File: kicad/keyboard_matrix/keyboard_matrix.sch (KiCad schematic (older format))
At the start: 21 parts, among them J1 Conn_01x09, SW1 SPST, SW10 SPST, SW11 SPST, SW12 SPST, SW13 SPST, SW14 SPST, SW15 SPST, SW16 SPST, SW17 SPST, SW18 SPST, SW19 SPST, SW2 SPST, SW20 SPST, SW3 SPST, SW4 SPST, SW5 SPST, SW6 SPST, SW7 SPST, SW8 SPST, SW9 SPST

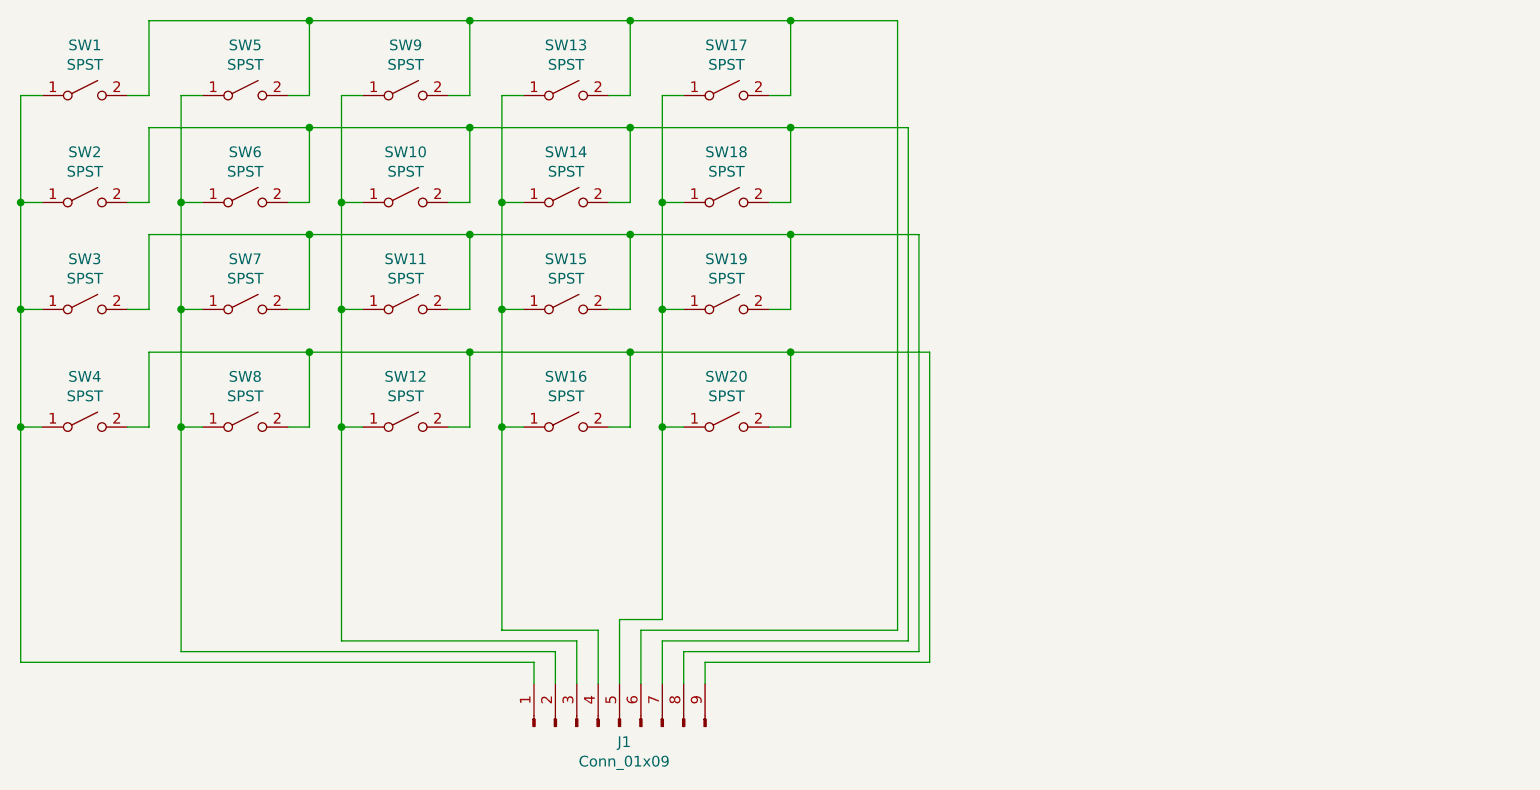
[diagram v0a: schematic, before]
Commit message: Try labels on matrix schematic
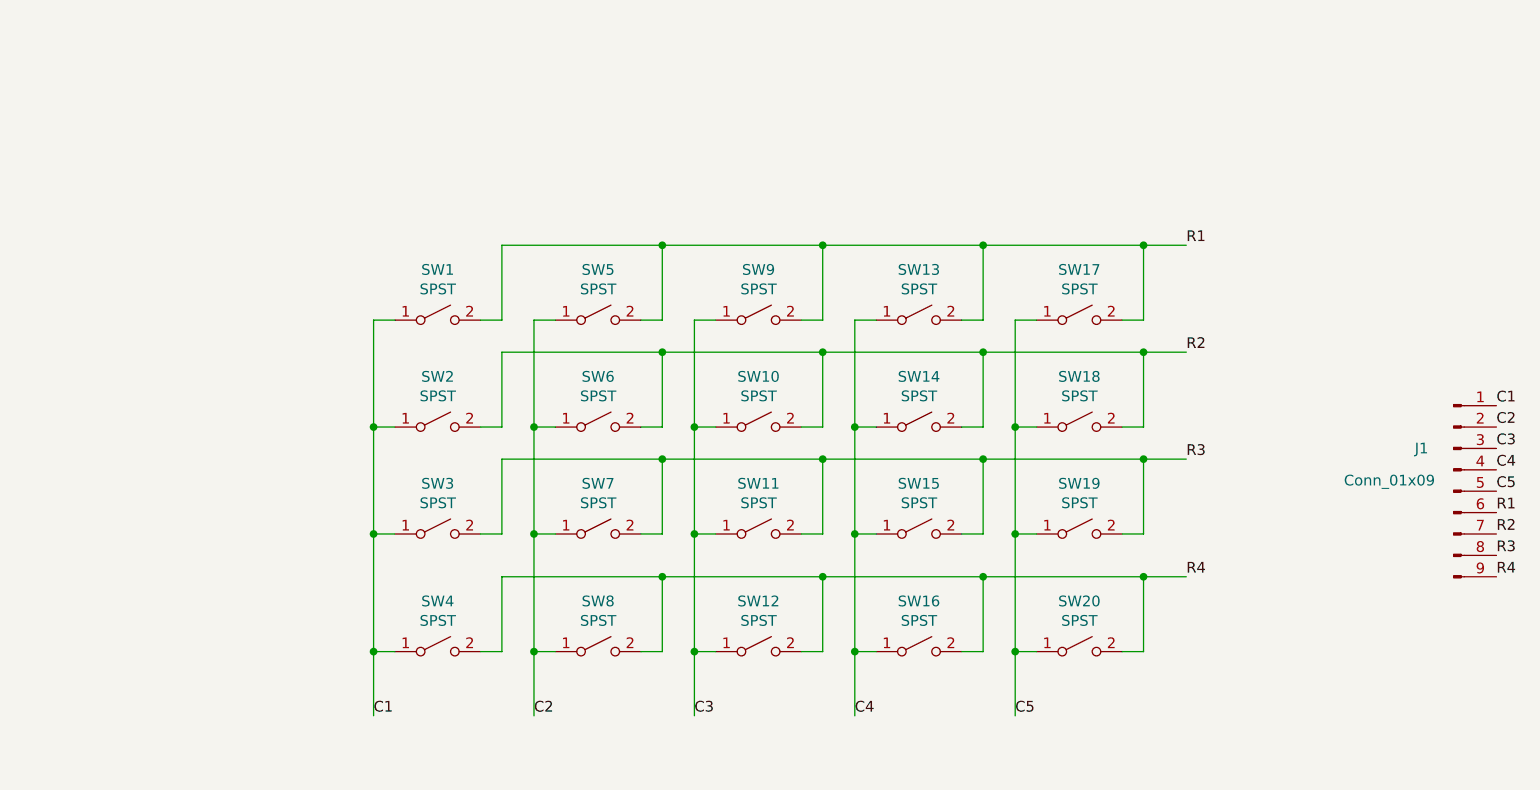
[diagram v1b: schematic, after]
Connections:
- net C1: now reaches J1.1 (Pin_1), SW1.1 (A), SW2.1 (A), SW3.1 (A), SW4.1 (A)
- net R1: now reaches J1.6 (Pin_6), SW1.2 (B), SW13.2 (B), SW17.2 (B), SW5.2 (B), SW9.2 (B)
- net C2: now reaches J1.2 (Pin_2), SW5.1 (A), SW6.1 (A), SW7.1 (A), SW8.1 (A)
- net C3: now reaches J1.3 (Pin_3), SW10.1 (A), SW11.1 (A), SW12.1 (A), SW9.1 (A)
- net C4: now reaches J1.4 (Pin_4), SW13.1 (A), SW14.1 (A), SW15.1 (A), SW16.1 (A)
- net C5: now reaches J1.5 (Pin_5), SW17.1 (A), SW18.1 (A), SW19.1 (A), SW20.1 (A)
- net R2: now reaches J1.7 (Pin_7), SW10.2 (B), SW14.2 (B), SW18.2 (B), SW2.2 (B), SW6.2 (B)
- net R3: now reaches J1.8 (Pin_8), SW11.2 (B), SW15.2 (B), SW19.2 (B), SW3.2 (B), SW7.2 (B)
- net R4: now reaches J1.9 (Pin_9), SW12.2 (B), SW16.2 (B), SW20.2 (B), SW4.2 (B), SW8.2 (B)
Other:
- moved on the sheet: J1, SW1, SW10, SW11, SW12, SW13, SW14, SW15, SW16, SW17, SW18, SW19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

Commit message: Draft matrix PCB
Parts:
- J1: footprint (none) -> Connector_PinHeader_2.54mm:PinHeader_1x09_P2.54mm_Horizontal
- SW1, SW10, SW11, SW12, SW13, SW14, SW15, SW16, SW17, SW18, SW19, SW2, SW20, SW3, SW4, SW5, SW6, SW7, SW8, SW9: footprint (none) -> Button_Switch_THT:SW_PUSH_6mm
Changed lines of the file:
@@
 F 0 "SW1" H 3700 3435 50  0000 C CNN
 F 1 "SPST" H 3700 3344 50  0000 C CNN
-F 2 "" H 3700 3200 50  0001 C CNN
+F 2 "Button_Switch_THT:SW_PUSH_6mm" H 3700 3200 50  0001 C CNN
 F 3 "~" H 3700 3200 50  0001 C CNN
 	1    3700 3200
@@
 F 0 "SW5" H 4450 3435 50  0000 C CNN
 F 1 "SPST" H 4450 3344 50  0000 C CNN
-F 2 "" H 4450 3200 50  0001 C CNN
+F 2 "Button_Switch_THT:SW_PUSH_6mm" H 4450 3200 50  0001 C CNN
 F 3 "~" H 4450 3200 50  0001 C CNN
 	1    4450 3200
@@
 F 0 "SW9" H 5200 3435 50  0000 C CNN
 F 1 "SPST" H 5200 3344 50  0000 C CNN
-F 2 "" H 5200 3200 50  0001 C CNN
+F 2 "Button_Switch_THT:SW_PUSH_6mm" H 5200 3200 50  0001 C CNN
 F 3 "~" H 5200 3200 50  0001 C CNN
 	1    5200 3200
@@
 F 0 "SW13" H 5950 3435 50  0000 C CNN
 F 1 "SPST" H 5950 3344 50  0000 C CNN
-F 2 "" H 5950 3200 50  0001 C CNN
+F 2 "Button_Switch_THT:SW_PUSH_6mm" H 5950 3200 50  0001 C CNN
 F 3 "~" H 5950 3200 50  0001 C CNN
 	1    5950 3200
@@
 F 0 "SW17" H 6700 3435 50  0000 C CNN
 F 1 "SPST" H 6700 3344 50  0000 C CNN
-F 2 "" H 6700 3200 50  0001 C CNN
+F 2 "Button_Switch_THT:SW_PUSH_6mm" H 6700 3200 50  0001 C CNN
 F 3 "~" H 6700 3200 50  0001 C CNN
 	1    6700 3200
@@
 F 0 "SW2" H 3700 3935 50  0000 C CNN
 F 1 "SPST" H 3700 3844 50  0000 C CNN
-F 2 "" H 3700 3700 50  0001 C CNN
+F 2 "Button_Switch_THT:SW_PUSH_6mm" H 3700 3700 50  0001 C CNN
 F 3 "~" H 3700 3700 50  0001 C CNN
 	1    3700 3700
@@
 F 0 "SW10" H 5200 3935 50  0000 C CNN
 F 1 "SPST" H 5200 3844 50  0000 C CNN
-F 2 "" H 5200 3700 50  0001 C CNN
+F 2 "Button_Switch_THT:SW_PUSH_6mm" H 5200 3700 50  0001 C CNN
 F 3 "~" H 5200 3700 50  0001 C CNN
 	1    5200 3700
@@
 F 0 "SW14" H 5950 3935 50  0000 C CNN
 F 1 "SPST" H 5950 3844 50  0000 C CNN
-F 2 "" H 5950 3700 50  0001 C CNN
+F 2 "Button_Switch_THT:SW_PUSH_6mm" H 5950 3700 50  0001 C CNN
 F 3 "~" H 5950 3700 50  0001 C CNN
 	1    5950 3700
@@
 F 0 "SW18" H 6700 3935 50  0000 C CNN
 F 1 "SPST" H 6700 3844 50  0000 C CNN
-F 2 "" H 6700 3700 50  0001 C CNN
+F 2 "Button_Switch_THT:SW_PUSH_6mm" H 6700 3700 50  0001 C CNN
 F 3 "~" H 6700 3700 50  0001 C CNN
 	1    6700 3700
@@
 F 0 "SW6" H 4450 3935 50  0000 C CNN
 F 1 "SPST" H 4450 3844 50  0000 C CNN
-F 2 "" H 4450 3700 50  0001 C CNN
+F 2 "Button_Switch_THT:SW_PUSH_6mm" H 4450 3700 50  0001 C CNN
 F 3 "~" H 4450 3700 50  0001 C CNN
 	1    4450 3700
@@
 F 0 "SW3" H 3700 4435 50  0000 C CNN
 F 1 "SPST" H 3700 4344 50  0000 C CNN
-F 2 "" H 3700 4200 50  0001 C CNN
+F 2 "Button_Switch_THT:SW_PUSH_6mm" H 3700 4200 50  0001 C CNN
 F 3 "~" H 3700 4200 50  0001 C CNN
 	1    3700 4200
@@
 F 0 "SW7" H 4450 4435 50  0000 C CNN
 F 1 "SPST" H 4450 4344 50  0000 C CNN
-F 2 "" H 4450 4200 50  0001 C CNN
+F 2 "Button_Switch_THT:SW_PUSH_6mm" H 4450 4200 50  0001 C CNN
 F 3 "~" H 4450 4200 50  0001 C CNN
 	1    4450 4200
@@
 F 0 "SW11" H 5200 4435 50  0000 C CNN
 F 1 "SPST" H 5200 4344 50  0000 C CNN
-F 2 "" H 5200 4200 50  0001 C CNN
+F 2 "Button_Switch_THT:SW_PUSH_6mm" H 5200 4200 50  0001 C CNN
 F 3 "~" H 5200 4200 50  0001 C CNN
 	1    5200 4200
@@
 F 0 "SW15" H 5950 4435 50  0000 C CNN
 F 1 "SPST" H 5950 4344 50  0000 C CNN
-F 2 "" H 5950 4200 50  0001 C CNN
+F 2 "Button_Switch_THT:SW_PUSH_6mm" H 5950 4200 50  0001 C CNN
 F 3 "~" H 5950 4200 50  0001 C CNN
 	1    5950 4200
@@
 F 0 "SW19" H 6700 4435 50  0000 C CNN
 F 1 "SPST" H 6700 4344 50  0000 C CNN
-F 2 "" H 6700 4200 50  0001 C CNN
+F 2 "Button_Switch_THT:SW_PUSH_6mm" H 6700 4200 50  0001 C CNN
 F 3 "~" H 6700 4200 50  0001 C CNN
 	1    6700 4200
@@
 F 0 "SW4" H 3700 4985 50  0000 C CNN
 F 1 "SPST" H 3700 4894 50  0000 C CNN
-F 2 "" H 3700 4750 50  0001 C CNN
+F 2 "Button_Switch_THT:SW_PUSH_6mm" H 3700 4750 50  0001 C CNN
 F 3 "~" H 3700 4750 50  0001 C CNN
 	1    3700 4750
@@
 F 0 "SW8" H 4450 4985 50  0000 C CNN
 F 1 "SPST" H 4450 4894 50  0000 C CNN
-F 2 "" H 4450 4750 50  0001 C CNN
+F 2 "Button_Switch_THT:SW_PUSH_6mm" H 4450 4750 50  0001 C CNN
 F 3 "~" H 4450 4750 50  0001 C CNN
 	1    4450 4750
@@
 F 0 "SW12" H 5200 4985 50  0000 C CNN
 F 1 "SPST" H 5200 4894 50  0000 C CNN
-F 2 "" H 5200 4750 50  0001 C CNN
+F 2 "Button_Switch_THT:SW_PUSH_6mm" H 5200 4750 50  0001 C CNN
 F 3 "~" H 5200 4750 50  0001 C CNN
 	1    5200 4750
@@
 F 0 "SW16" H 5950 4985 50  0000 C CNN
 F 1 "SPST" H 5950 4894 50  0000 C CNN
-F 2 "" H 5950 4750 50  0001 C CNN
+F 2 "Button_Switch_THT:SW_PUSH_6mm" H 5950 4750 50  0001 C CNN
 F 3 "~" H 5950 4750 50  0001 C CNN
 	1    5950 4750
@@
 F 0 "SW20" H 6700 4985 50  0000 C CNN
 F 1 "SPST" H 6700 4894 50  0000 C CNN
-F 2 "" H 6700 4750 50  0001 C CNN
+F 2 "Button_Switch_THT:SW_PUSH_6mm" H 6700 4750 50  0001 C CNN
 F 3 "~" H 6700 4750 50  0001 C CNN
 	1    6700 4750
@@
 F 0 "J1" H 8300 4200 50  0000 C CNN
 F 1 "Conn_01x09" H 8150 4050 50  0000 C CNN
-F 2 "" H 8450 4000 50  0001 C CNN
+F 2 "Connector_PinHeader_2.54mm:PinHeader_1x09_P2.54mm_Horizontal" H 8450 4000 50  0001 C CNN
 F 3 "~" H 8450 4000 50  0001 C CNN
 	1    8450 4000
